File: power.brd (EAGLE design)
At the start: 90 x 77.5 mm, 37 parts, among them IC1 74HC125D, IC2 7805TV, IC3 7815TV

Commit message: wait for the next one...
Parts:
- removed D5: AA215, diode:DO07
- added OK1: 4N35M, optocoupler:DIL06
- D4: value AA215 -> 1N4446; device diode:DO07 -> diode:DO35-10
- moved D4 51.6 mm to (-7.50, -6.50), turned to 0 degrees
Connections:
- removed net N$14: D4.C, D5.A, U$6.80
- new net N$31: OK1.1, R12.2
- net GND: now also OK1.2, OK1.6, U$6.86
- net N$26: now also D4.C, OK1.5, U$6.80; no longer D5.C, R12.1
- net N$8: no longer R12.2
- net VCC: now also R12.1
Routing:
- net N$14: track 32.7 -> 0.00 mm
- net N$26: track 11.1 -> 23.3 mm
- net N$8: track 35.5 -> 32.1 mm
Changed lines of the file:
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@@
 <?xml version="1.0" encoding="utf-8"?>
 <!DOCTYPE eagle SYSTEM "eagle.dtd">
-<eagle version="6.5.0">
+<eagle version="6.5.1">
 <drawing>
 <settings>
@@
 <element name="H3" library="holes" package="2,8-PAD" value="MOUNT-PAD-ROUND2.8" x="67.5" y="70"/>
 <element name="R7" library="rcl" package="R0603" value="15k" x="75" y="4" rot="MR0"/>
-<element name="D4" library="diode" package="DO07" value="AA215" x="36.5" y="20.5" rot="R180"/>
 <element name="R12" library="rcl" package="R0603" value="1k" x="35" y="37.5" rot="MR90"/>
 <element name="IC1" library="74xx-eu" package="SO14" value="74HC125D" x="51" y="5.5" rot="R180"/>
@@
 <element name="SJ3" library="jumper" package="SJ_2" value="" x="29" y="8"/>
 <element name="SJ4" library="jumper" package="SJ_2" value="" x="41" y="8"/>
-<element name="D5" library="diode" package="DO07" value="AA215" x="36.5" y="27"/>
+<element name="OK1" library="optocoupler" package="DIL06" value="4N35M" x="-9" y="4">
+<attribute name="OC_NEWARK" value="98K9114" x="-9" y="4" size="1.778" layer="27" display="off"/>
+<attribute name="MPN" value="4N35-M" x="-9" y="4" size="1.778" layer="27" display="off"/>
+<attribute name="MF" value="" x="-9" y="4" size="1.778" layer="27" display="off"/>
+<attribute name="OC_FARNELL" value="1021351" x="-9" y="4" size="1.778" layer="27" display="off"/>
+</element>
+<element name="D4" library="diode" package="DO35-10" value="1N4446" x="-7.5" y="-6.5"/>
 </elements>
 <signals>
@@
 <contactref element="H2" pad="B2,8"/>
 <contactref element="H3" pad="B2,8"/>
-<contactref element="D4" pad="A"/>
 <contactref element="IC1" pad="4"/>
 <contactref element="IC1" pad="1"/>
@@
 <contactref element="U$5" pad="P$1"/>
 <contactref element="U$4" pad="P$4"/>
+<contactref element="OK1" pad="2"/>
+<contactref element="D4" pad="A"/>
+<contactref element="OK1" pad="6"/>
+<contactref element="U$6" pad="86"/>
+<wire x1="73.65" y1="56.5" x2="67.5" y2="70" width="0" layer="19" extent="16-16"/>
+<wire x1="72.46" y1="43" x2="73.65" y2="56.5" width="0" layer="19" extent="16-16"/>
+<wire x1="63" y1="44" x2="72.46" y2="43" width="0" layer="19" extent="1-1"/>
+<wire x1="63" y1="35.5" x2="63" y2="44" width="0" layer="19" extent="1-1"/>
+<wire x1="66.31" y1="14.835" x2="63" y2="35.5" width="0" layer="19" extent="1-1"/>
+<wire x1="71.39" y1="14.835" x2="66.31" y2="14.835" width="0" layer="19" extent="1-1"/>
+<wire x1="73.93" y1="14.835" x2="71.39" y2="14.835" width="0" layer="19" extent="1-1"/>
+<wire x1="73.93" y1="12.295" x2="73.93" y2="14.835" width="0" layer="19" extent="1-1"/>
+<wire x1="71.39" y1="12.295" x2="71.39" y2="14.835" width="0" layer="19" extent="1-1"/>
+<wire x1="75.85" y1="6" x2="73.93" y2="12.295" width="0" layer="19" extent="16-16"/>
+<wire x1="62.5" y1="5" x2="66.31" y2="14.835" width="0" layer="19" extent="1-1"/>
+<wire x1="56.5" y1="2.5" x2="62.5" y2="5" width="0" layer="19" extent="1-1"/>
+<wire x1="49.73" y1="2.4266" x2="53.54" y2="2.4266" width="0" layer="19" extent="1-1"/>
+<wire x1="50" y1="6.5" x2="49.73" y2="2.4266" width="0" layer="19" extent="1-1"/>
+<wire x1="47.5" y1="6.5" x2="50" y2="6.5" width="0" layer="19" extent="1-16"/>
+<wire x1="30.5" y1="31.25" x2="45.5" y2="8.5" width="0" layer="19" extent="1-1"/>
+<wire x1="15" y1="37.85" x2="30.5" y2="31.25" width="0" layer="19" extent="16-16"/>
+<wire x1="7.65" y1="35.5" x2="15" y2="37.85" width="0" layer="19" extent="16-16"/>
+<wire x1="6.5" y1="53.96" x2="15" y2="37.85" width="0" layer="19" extent="16-16"/>
+<wire x1="6.5" y1="62.54" x2="6.5" y2="53.96" width="0" layer="19" extent="1-1"/>
+<wire x1="5" y1="70" x2="6.5" y2="62.54" width="0" layer="19" extent="1-1"/>
+<wire x1="18.05" y1="63.095" x2="6.5" y2="62.54" width="0" layer="19" extent="1-1"/>
+<wire x1="18.05" y1="60.555" x2="18.05" y2="63.095" width="0" layer="19" extent="1-1"/>
+<wire x1="18.05" y1="14.835" x2="30.5" y2="31.25" width="0" layer="19" extent="1-1"/>
+<wire x1="18.05" y1="12.295" x2="18.05" y2="14.835" width="0" layer="19" extent="1-1"/>
+<wire x1="9.15" y1="6" x2="18.05" y2="12.295" width="0" layer="19" extent="16-16"/>
+<wire x1="-2.42" y1="-6.5" x2="9.15" y2="6" width="0" layer="19" extent="16-16"/>
+<wire x1="-9" y1="0.19" x2="-2.42" y2="-6.5" width="0" layer="19" extent="1-1"/>
+<wire x1="-11.54" y1="7.81" x2="-9" y2="0.19" width="0" layer="19" extent="1-1"/>
 </signal>
 <signal name="VDD_3V3EXP">
@@
 <wire x1="13" y1="39.85" x2="12.95" y2="40" width="1.016" layer="16"/>
 <wire x1="20.96" y1="40.69" x2="20.27" y2="40" width="1.016" layer="16"/>
-<contactref element="R12" pad="2"/>
-<wire x1="35" y1="38.35" x2="31.65" y2="38.35" width="0.3048" layer="16"/>
 <wire x1="31.65" y1="38.35" x2="27" y2="43" width="0.3048" layer="16"/>
 <wire x1="27" y1="43" x2="23.27" y2="43" width="0.3048" layer="16"/>
@@
 <wire x1="18" y1="-1" x2="13" y2="4" width="0.3048" layer="16"/>
 <wire x1="13" y1="4" x2="10.85" y2="4" width="0.3048" layer="16"/>
-</signal>
-<signal name="N$14">
-<contactref element="U$6" pad="80"/>
-<contactref element="D4" pad="C"/>
-<wire x1="58.69" y1="14.835" x2="58.69" y2="18.81" width="0.3048" layer="16"/>
-<contactref element="D5" pad="A"/>
-<wire x1="41.58" y1="20.5" x2="48" y2="20.5" width="0.3048" layer="16"/>
-<wire x1="48" y1="20.5" x2="57" y2="20.5" width="0.3048" layer="16"/>
-<wire x1="57" y1="20.5" x2="58.69" y2="18.81" width="0.3048" layer="16"/>
-<wire x1="41.58" y1="27" x2="44.5" y2="27" width="0.3048" layer="16"/>
-<wire x1="44.5" y1="27" x2="48" y2="23.5" width="0.3048" layer="16"/>
-<wire x1="48" y1="23.5" x2="48" y2="20.5" width="0.3048" layer="16"/>
 </signal>
 <signal name="N$27">
@@
 <wire x1="23.13" y1="14.835" x2="23.13" y2="39.87" width="0.4064" layer="1"/>
 <wire x1="23.13" y1="39.87" x2="9.04" y2="53.96" width="0.4064" layer="1"/>
+<contactref element="R12" pad="1"/>
+<wire x1="23.13" y1="39.87" x2="35" y2="36.65" width="0" layer="19" extent="1-16"/>
 </signal>
 <signal name="N$1">
@@
 <wire x1="40.5" y1="31.25" x2="66.63" y2="31.25" width="2.54" layer="16"/>
 <wire x1="66.63" y1="31.25" x2="67.38" y2="32" width="2.54" layer="16"/>
-</signal>
-<signal name="N$26">
-<contactref element="R12" pad="1"/>
-<contactref element="D5" pad="C"/>
-<wire x1="35" y1="36.65" x2="35" y2="30.58" width="0.3048" layer="16"/>
-<wire x1="35" y1="30.58" x2="31.42" y2="27" width="0.3048" layer="16"/>
 </signal>
 <signal name="N$20">
@@
 <wire x1="45.0734" y1="2.4266" x2="47.19" y2="2.4266" width="0.3048" layer="1"/>
 </signal>
+<signal name="N$26">
+<contactref element="OK1" pad="5"/>
+<contactref element="D4" pad="C"/>
+<contactref element="U$6" pad="80"/>
+<wire x1="58.69" y1="14.835" x2="58.69" y2="18.81" width="0.3048" layer="16"/>
+<wire x1="48" y1="20.5" x2="57" y2="20.5" width="0.3048" layer="16"/>
+<wire x1="57" y1="20.5" x2="58.69" y2="18.81" width="0.3048" layer="16"/>
+<wire x1="44.5" y1="27" x2="48" y2="23.5" width="0.3048" layer="16"/>
+<wire x1="48" y1="23.5" x2="48" y2="20.5" width="0.3048" layer="16"/>
+<wire x1="-9" y1="7.81" x2="44.5" y2="27" width="0" layer="19" extent="16-16"/>
+<wire x1="-12.58" y1="-6.5" x2="-9" y2="7.81" width="0" layer="19" extent="1-1"/>
+</signal>
+<signal name="N$31">
+<contactref element="R12" pad="2"/>
+<contactref element="OK1" pad="1"/>
+<wire x1="-11.54" y1="0.19" x2="35" y2="38.35" width="0" layer="19" extent="16-16"/>
+</signal>
 </signals>

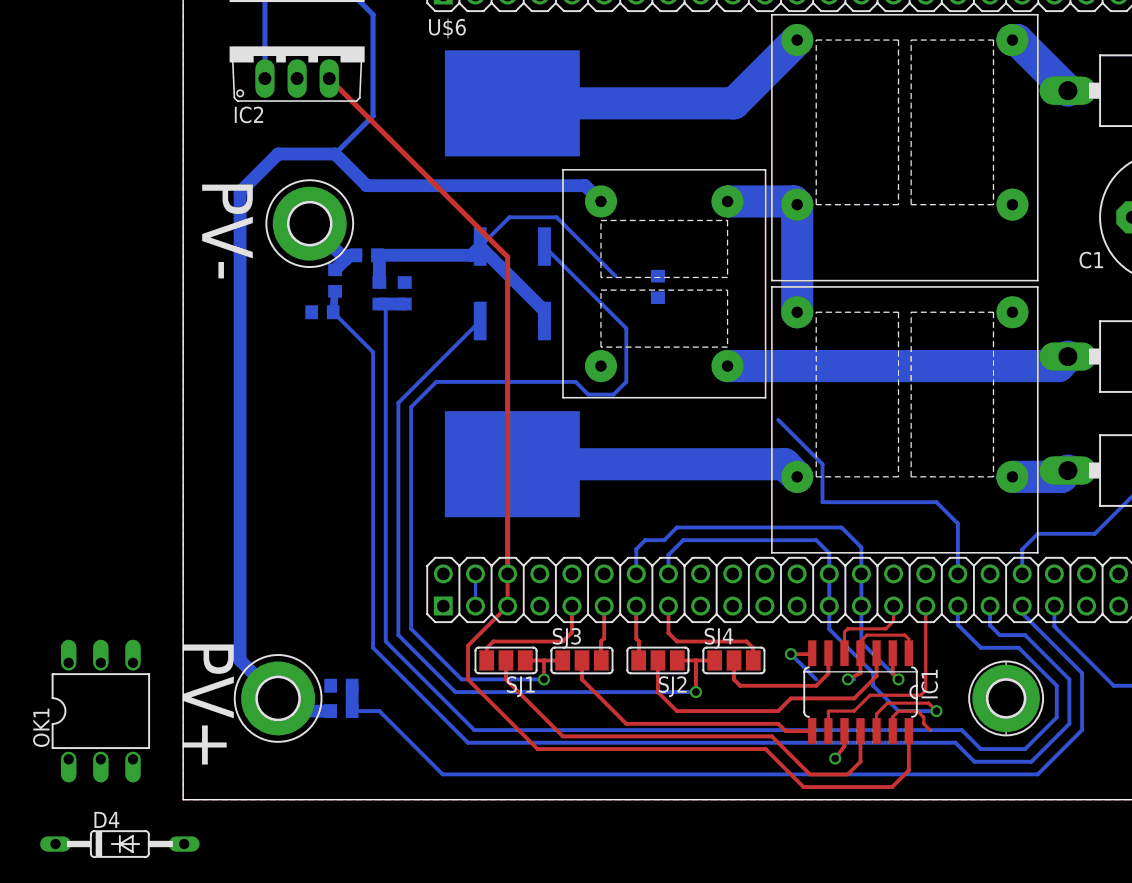
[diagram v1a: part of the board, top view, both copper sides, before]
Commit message: Removing all the failed ideas
Everything may be broken
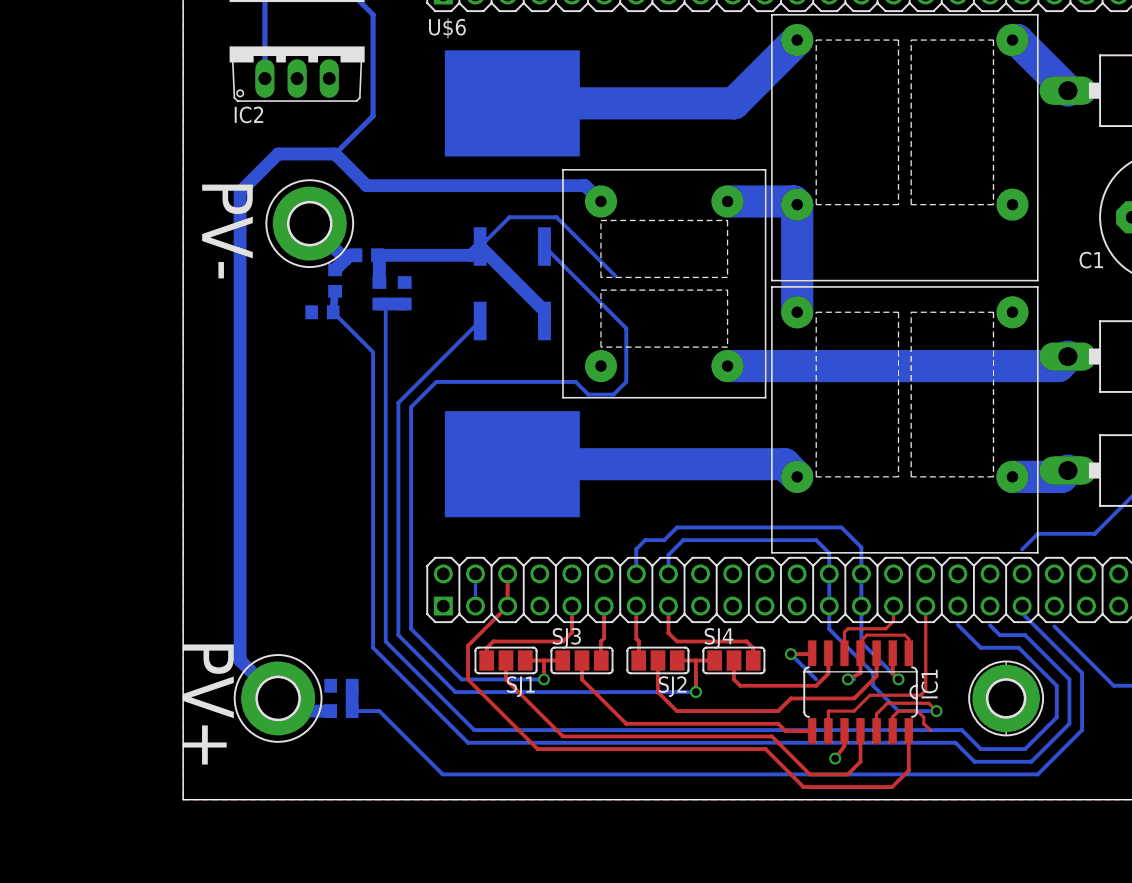
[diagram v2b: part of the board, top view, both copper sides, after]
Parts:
- removed D4: 1N4446, diode:DO35-10
- removed OK1: 4N35M, optocoupler:DIL06
- removed R12: 1k, rcl:R0603
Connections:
- removed net N$26: D4.C, OK1.5, U$6.80
- removed net N$31: OK1.1, R12.2
- new net AIN0: U$6.85
- net GND: no longer D4.A, OK1.2, OK1.6, U$6.86
- net N$10: no longer U$6.85
- net N$12: no longer U$6.83
- net N$17: no longer U$6.81
- net N$18: no longer U$6.79
- net N$4: no longer U$6.84
- net VCC: no longer R12.1
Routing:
- net VCC: track 96.6 -> 51.6 mm
- net N$26: track 23.3 -> 0.00 mm
- net N$4: track 66.6 -> 64.7 mm
- net N$10: track 13.4 -> 11.8 mm
- net N$17: track 102.9 -> 101.3 mm
- net N$18: track 101.0 -> 99.5 mm
- net N$12: track 74.9 -> 74.4 mm
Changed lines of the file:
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@@
 <element name="H3" library="holes" package="2,8-PAD" value="MOUNT-PAD-ROUND2.8" x="67.5" y="70"/>
 <element name="R7" library="rcl" package="R0603" value="15k" x="75" y="4" rot="MR0"/>
-<element name="R12" library="rcl" package="R0603" value="1k" x="35" y="37.5" rot="MR90"/>
 <element name="IC1" library="74xx-eu" package="SO14" value="74HC125D" x="51" y="5.5" rot="R180"/>
 <element name="IC2" library="linear" package="TO220V" value="7805TV" x="6.5" y="56.5"/>
@@
 <element name="SJ3" library="jumper" package="SJ_2" value="" x="29" y="8"/>
 <element name="SJ4" library="jumper" package="SJ_2" value="" x="41" y="8"/>
-<element name="OK1" library="optocoupler" package="DIL06" value="4N35M" x="-9" y="4">
-<attribute name="OC_NEWARK" value="98K9114" x="-9" y="4" size="1.778" layer="27" display="off"/>
-<attribute name="MPN" value="4N35-M" x="-9" y="4" size="1.778" layer="27" display="off"/>
-<attribute name="MF" value="" x="-9" y="4" size="1.778" layer="27" display="off"/>
-<attribute name="OC_FARNELL" value="1021351" x="-9" y="4" size="1.778" layer="27" display="off"/>
-</element>
-<element name="D4" library="diode" package="DO35-10" value="1N4446" x="-7.5" y="-6.5"/>
 </elements>
 <signals>
@@
 <contactref element="U$5" pad="P$1"/>
 <contactref element="U$4" pad="P$4"/>
-<contactref element="OK1" pad="2"/>
-<contactref element="D4" pad="A"/>
-<contactref element="OK1" pad="6"/>
-<contactref element="U$6" pad="86"/>
 <wire x1="73.65" y1="56.5" x2="67.5" y2="70" width="0" layer="19" extent="16-16"/>
 <wire x1="72.46" y1="43" x2="73.65" y2="56.5" width="0" layer="19" extent="16-16"/>
 <wire x1="63" y1="44" x2="72.46" y2="43" width="0" layer="19" extent="1-1"/>
 <wire x1="63" y1="35.5" x2="63" y2="44" width="0" layer="19" extent="1-1"/>
-<wire x1="66.31" y1="14.835" x2="63" y2="35.5" width="0" layer="19" extent="1-1"/>
-<wire x1="71.39" y1="14.835" x2="66.31" y2="14.835" width="0" layer="19" extent="1-1"/>
+<wire x1="71.39" y1="14.835" x2="63" y2="35.5" width="0" layer="19" extent="1-1"/>
 <wire x1="73.93" y1="14.835" x2="71.39" y2="14.835" width="0" layer="19" extent="1-1"/>
 <wire x1="73.93" y1="12.295" x2="73.93" y2="14.835" width="0" layer="19" extent="1-1"/>
 <wire x1="71.39" y1="12.295" x2="71.39" y2="14.835" width="0" layer="19" extent="1-1"/>
 <wire x1="75.85" y1="6" x2="73.93" y2="12.295" width="0" layer="19" extent="16-16"/>
-<wire x1="62.5" y1="5" x2="66.31" y2="14.835" width="0" layer="19" extent="1-1"/>
+<wire x1="62.5" y1="5" x2="71.39" y2="12.295" width="0" layer="19" extent="1-1"/>
 <wire x1="56.5" y1="2.5" x2="62.5" y2="5" width="0" layer="19" extent="1-1"/>
 <wire x1="49.73" y1="2.4266" x2="53.54" y2="2.4266" width="0" layer="19" extent="1-1"/>
@@
 <wire x1="18.05" y1="12.295" x2="18.05" y2="14.835" width="0" layer="19" extent="1-1"/>
 <wire x1="9.15" y1="6" x2="18.05" y2="12.295" width="0" layer="19" extent="16-16"/>
-<wire x1="-2.42" y1="-6.5" x2="9.15" y2="6" width="0" layer="19" extent="16-16"/>
-<wire x1="-9" y1="0.19" x2="-2.42" y2="-6.5" width="0" layer="19" extent="1-1"/>
-<wire x1="-11.54" y1="7.81" x2="-9" y2="0.19" width="0" layer="19" extent="1-1"/>
 </signal>
 <signal name="VDD_3V3EXP">
@@
 </signal>
 <signal name="N$4">
-<contactref element="U$6" pad="84"/>
 <contactref element="R1" pad="2"/>
 <contactref element="BAT-" pad="B2,8"/>
@@
 <wire x1="75" y1="23.5" x2="69.5" y2="18" width="0.3048" layer="16"/>
 <wire x1="69.5" y1="18" x2="65" y2="18" width="0.3048" layer="16"/>
-<wire x1="63.77" y1="14.835" x2="63.77" y2="16.77" width="0.3048" layer="16"/>
 <wire x1="63.77" y1="16.77" x2="65" y2="18" width="0.3048" layer="16"/>
 <wire x1="75" y1="52.5" x2="75" y2="23.5" width="0.3048" layer="16"/>
@@
 <contactref element="R5" pad="2"/>
 <contactref element="R6" pad="2"/>
-<contactref element="U$6" pad="81"/>
 <wire x1="9.5" y1="37.15" x2="9.35" y2="35.5" width="0.6096" layer="16"/>
 <wire x1="9.35" y1="35.5" x2="9.15" y2="35.8" width="0.254" layer="16"/>
-<wire x1="61.23" y1="12.295" x2="61.23" y2="10.77" width="0.3048" layer="16"/>
 <wire x1="61.23" y1="10.77" x2="62" y2="10" width="0.3048" layer="16"/>
 <wire x1="62" y1="10" x2="64" y2="10" width="0.3048" layer="16"/>
@@
 </signal>
 <signal name="N$18">
-<contactref element="U$6" pad="79"/>
 <contactref element="R9" pad="2"/>
 <contactref element="R10" pad="2"/>
@@
 <wire x1="13.5" y1="36.5" x2="13.15" y2="36.15" width="0.3048" layer="16"/>
 <wire x1="13.15" y1="36.15" x2="13" y2="36.15" width="0.3048" layer="16"/>
-<wire x1="58.69" y1="12.295" x2="58.69" y2="10.81" width="0.3048" layer="16"/>
 <wire x1="58.69" y1="10.81" x2="60.5" y2="9" width="0.3048" layer="16"/>
 <wire x1="60.5" y1="9" x2="63.5" y2="9" width="0.3048" layer="16"/>
@@
 <contactref element="R8" pad="2"/>
 <contactref element="R7" pad="2"/>
-<contactref element="U$6" pad="85"/>
 <wire x1="74.15" y1="4" x2="74.15" y2="6" width="1.016" layer="16"/>
 <wire x1="74.15" y1="6" x2="71" y2="6" width="0.3048" layer="16"/>
 <wire x1="71" y1="6" x2="66.31" y2="10.69" width="0.3048" layer="16"/>
-<wire x1="66.31" y1="10.69" x2="66.31" y2="12.295" width="0.3048" layer="16"/>
 </signal>
 <signal name="N$12">
@@
 <contactref element="R4" pad="2"/>
 <wire x1="10.85" y1="6" x2="10.85" y2="4" width="1.016" layer="16"/>
-<contactref element="U$6" pad="83"/>
-<wire x1="63.77" y1="12.295" x2="63.77" y2="11.73" width="0.3048" layer="16"/>
 <wire x1="63.77" y1="11.73" x2="68.5" y2="7" width="0.3048" layer="16"/>
 <wire x1="68.5" y1="7" x2="68.5" y2="2.5" width="0.3048" layer="16"/>
@@
 <wire x1="20" y1="9.165" x2="23.13" y2="12.295" width="0.3048" layer="1"/>
 <wire x1="23.13" y1="12.295" x2="23.13" y2="14.835" width="0.3048" layer="1"/>
-<wire x1="23.13" y1="14.835" x2="23.13" y2="39.87" width="0.4064" layer="1"/>
-<wire x1="23.13" y1="39.87" x2="9.04" y2="53.96" width="0.4064" layer="1"/>
-<contactref element="R12" pad="1"/>
-<wire x1="23.13" y1="39.87" x2="35" y2="36.65" width="0" layer="19" extent="1-16"/>
+<wire x1="23.13" y1="14.835" x2="9.04" y2="53.96" width="0" layer="19" extent="1-1"/>
 </signal>
 <signal name="N$1">
@@
 <wire x1="45.0734" y1="2.4266" x2="47.19" y2="2.4266" width="0.3048" layer="1"/>
 </signal>
-<signal name="N$26">
-<contactref element="OK1" pad="5"/>
-<contactref element="D4" pad="C"/>
-<contactref element="U$6" pad="80"/>
-<wire x1="58.69" y1="14.835" x2="58.69" y2="18.81" width="0.3048" layer="16"/>
-<wire x1="48" y1="20.5" x2="57" y2="20.5" width="0.3048" layer="16"/>
-<wire x1="57" y1="20.5" x2="58.69" y2="18.81" width="0.3048" layer="16"/>
-<wire x1="44.5" y1="27" x2="48" y2="23.5" width="0.3048" layer="16"/>
-<wire x1="48" y1="23.5" x2="48" y2="20.5" width="0.3048" layer="16"/>
-<wire x1="-9" y1="7.81" x2="44.5" y2="27" width="0" layer="19" extent="16-16"/>
-<wire x1="-12.58" y1="-6.5" x2="-9" y2="7.81" width="0" layer="19" extent="1-1"/>
-</signal>
-<signal name="N$31">
-<contactref element="R12" pad="2"/>
-<contactref element="OK1" pad="1"/>
-<wire x1="-11.54" y1="0.19" x2="35" y2="38.35" width="0" layer="19" extent="16-16"/>
+<signal name="AIN0">
+<contactref element="U$6" pad="85"/>
 </signal>
 </signals>
